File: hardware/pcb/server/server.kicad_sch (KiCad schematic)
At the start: 11 parts

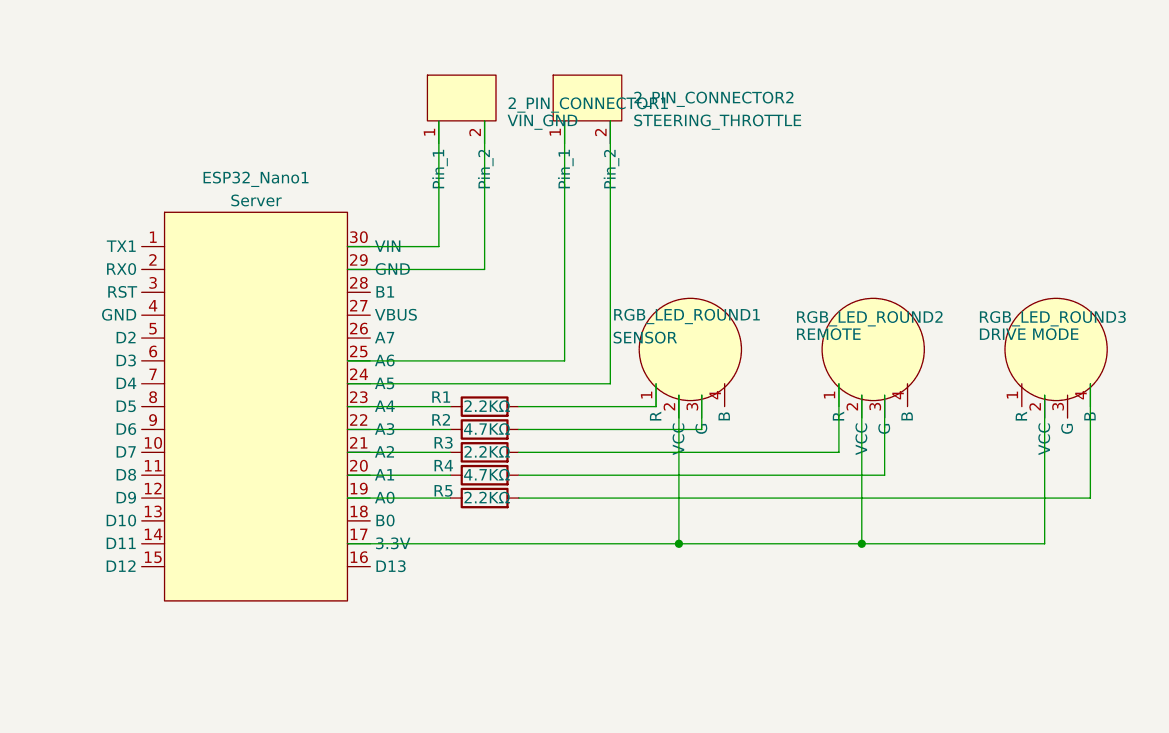
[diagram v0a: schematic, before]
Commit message: hardware/pcb/server: Update pcb pins for the server.
Update the wiring accordingly to use D2-D8 pins.
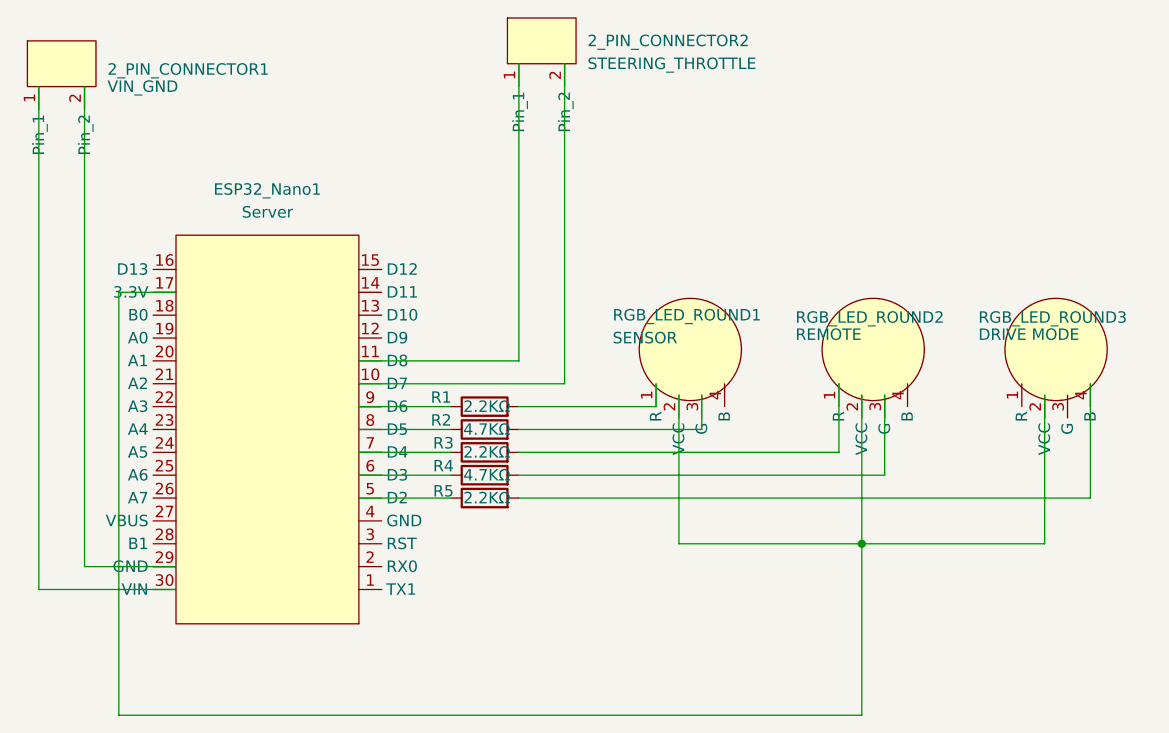
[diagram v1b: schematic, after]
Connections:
- net at ESP32_Nano1.10 (D7): now also 2_PIN_CONNECTOR2.2 (Pin_2)
- net at ESP32_Nano1.11 (D8): now also 2_PIN_CONNECTOR2.1 (Pin_1)
- net at ESP32_Nano1.19 (A0): no longer R5.1
- net at ESP32_Nano1.20 (A1): no longer R4.1
- net at ESP32_Nano1.21 (A2): no longer R3.1
- net at ESP32_Nano1.22 (A3): no longer R2.1
- net at ESP32_Nano1.23 (A4): no longer R1.1
- net at ESP32_Nano1.24 (A5): no longer 2_PIN_CONNECTOR2.2 (Pin_2)
- net at ESP32_Nano1.25 (A6): no longer 2_PIN_CONNECTOR2.1 (Pin_1)
- net at ESP32_Nano1.5 (D2): now also R5.1
- net at ESP32_Nano1.6 (D3): now also R4.1
- net at ESP32_Nano1.7 (D4): now also R3.1
- net at ESP32_Nano1.8 (D5): now also R2.1
- net at ESP32_Nano1.9 (D6): now also R1.1
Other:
- moved on the sheet: 2_PIN_CONNECTOR1, 2_PIN_CONNECTOR2, ESP32_Nano1
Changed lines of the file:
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@@
 	(title_block
 		(title "Autocam Server")
-		(date "2025-03-18")
-		(rev "v0.2")
+		(date "2025-05-21")
+		(rev "v0.3")
 	)
 	(junction
@@
 		(color 0 0 0 0)
 	)
-	(junction
-		(at 165.1 119.38)
-		(diameter 0)
-		(color 0 0 0 0)
-	)
 	(wire
 		(pts
@@
 	(wire
 		(pts
-			(xy 143.51 88.9) (xy 128.27 88.9)
+			(xy 129.54 106.68) (xy 139.7 106.68)
 		)
 		(stroke
@@
 	(wire
 		(pts
-			(xy 128.27 111.76) (xy 139.7 111.76)
-		)
-		(stroke
-			(width 0)
-			(type default)
-		)
-	)
-	(wire
-		(pts
 			(xy 185.42 119.38) (xy 205.74 119.38)
 		)
@@
 	(wire
 		(pts
-			(xy 143.51 72.39) (xy 143.51 88.9)
-		)
-		(stroke
-			(width 0)
-			(type default)
-		)
-	)
-	(wire
-		(pts
-			(xy 157.48 72.39) (xy 157.48 101.6)
-		)
-		(stroke
-			(width 0)
-			(type default)
-		)
-	)
-	(wire
-		(pts
-			(xy 138.43 72.39) (xy 138.43 86.36)
-		)
-		(stroke
-			(width 0)
-			(type default)
-		)
-	)
-	(wire
-		(pts
-			(xy 128.27 114.3) (xy 139.7 114.3)
-		)
-		(stroke
-			(width 0)
-			(type default)
-		)
-	)
-	(wire
-		(pts
-			(xy 128.27 101.6) (xy 157.48 101.6)
-		)
-		(stroke
-			(width 0)
-			(type default)
-		)
-	)
-	(wire
-		(pts
-			(xy 128.27 119.38) (xy 165.1 119.38)
+			(xy 185.42 138.43) (xy 102.87 138.43)
+		)
+		(stroke
+			(width 0)
+			(type default)
+		)
+	)
+	(wire
+		(pts
+			(xy 129.54 109.22) (xy 139.7 109.22)
+		)
+		(stroke
+			(width 0)
+			(type default)
+		)
+	)
+	(wire
+		(pts
+			(xy 102.87 138.43) (xy 102.87 91.44)
+		)
+		(stroke
+			(width 0)
+			(type default)
+		)
+	)
+	(wire
+		(pts
+			(xy 93.98 124.46) (xy 109.22 124.46)
+		)
+		(stroke
+			(width 0)
+			(type default)
+		)
+	)
+	(wire
+		(pts
+			(xy 152.4 101.6) (xy 129.54 101.6)
+		)
+		(stroke
+			(width 0)
+			(type default)
+		)
+	)
+	(wire
+		(pts
+			(xy 129.54 114.3) (xy 139.7 114.3)
+		)
+		(stroke
+			(width 0)
+			(type default)
+		)
+	)
+	(wire
+		(pts
+			(xy 152.4 66.04) (xy 152.4 101.6)
+		)
+		(stroke
+			(width 0)
+			(type default)
+		)
+	)
+	(wire
+		(pts
+			(xy 185.42 119.38) (xy 185.42 138.43)
 		)
 		(stroke
@@
 	(wire
 		(pts
+			(xy 102.87 91.44) (xy 109.22 91.44)
+		)
+		(stroke
+			(width 0)
+			(type default)
+		)
+	)
+	(wire
+		(pts
 			(xy 162.56 101.6) (xy 162.56 104.14)
 		)
@@
 	(wire
 		(pts
-			(xy 138.43 86.36) (xy 128.27 86.36)
-		)
-		(stroke
-			(width 0)
-			(type default)
-		)
-	)
-	(wire
-		(pts
 			(xy 182.88 101.6) (xy 182.88 109.22)
 		)
@@
 	(wire
 		(pts
+			(xy 93.98 68.58) (xy 93.98 124.46)
+		)
+		(stroke
+			(width 0)
+			(type default)
+		)
+	)
+	(wire
+		(pts
 			(xy 147.32 111.76) (xy 187.96 111.76)
 		)
@@
 	(wire
 		(pts
-			(xy 139.7 104.14) (xy 128.27 104.14)
-		)
-		(stroke
-			(width 0)
-			(type default)
-		)
-	)
-	(wire
-		(pts
-			(xy 139.7 109.22) (xy 128.27 109.22)
+			(xy 147.32 66.04) (xy 147.32 99.06)
+		)
+		(stroke
+			(width 0)
+			(type default)
+		)
+	)
+	(wire
+		(pts
+			(xy 99.06 68.58) (xy 99.06 121.92)
 		)
 		(stroke
@@
 	(wire
 		(pts
-			(xy 152.4 72.39) (xy 152.4 99.06)
-		)
-		(stroke
-			(width 0)
-			(type default)
-		)
-	)
-	(wire
-		(pts
-			(xy 128.27 106.68) (xy 139.7 106.68)
+			(xy 129.54 111.76) (xy 139.7 111.76)
 		)
 		(stroke
@@
 	(wire
 		(pts
+			(xy 147.32 99.06) (xy 129.54 99.06)
+		)
+		(stroke
+			(width 0)
+			(type default)
+		)
+	)
+	(wire
+		(pts
 			(xy 187.96 102.87) (xy 187.96 111.76)
 		)
@@
 	(wire
 		(pts
-			(xy 152.4 99.06) (xy 128.27 99.06)
+			(xy 129.54 104.14) (xy 139.7 104.14)
 		)
 		(stroke
@@
 		(pts
 			(xy 147.32 114.3) (xy 210.82 114.3)
+		)
+		(stroke
+			(width 0)
+			(type default)
+		)
+	)
+	(wire
+		(pts
+			(xy 99.06 121.92) (xy 109.22 121.92)
 		)
 		(stroke
@@
 	(symbol
 		(lib_id "Autocam:2_PIN_Connector")
-		(at 140.97 69.85 0)
+		(at 96.52 66.04 0)
 		(unit 1)
 		(exclude_from_sim no)
@@
 		(on_board yes)
 		(dnp no)
-		(fields_autoplaced yes)
 		(property "Reference" "2_PIN_CONNECTOR1"
-			(at 146.05 70.4849 0)
+			(at 101.6 66.6749 0)
 			(effects
 				(font
@@
 		)
 		(property "Value" "VIN_GND"
-			(at 146.05 72.39 0)
+			(at 101.6 68.58 0)
 			(effects
 				(font
@@
 		)
 		(property "Footprint" "Autocam:2-PIN Connector"
-			(at 140.97 69.85 0)
+			(at 96.52 66.04 0)
 			(effects
 				(font
@@
 		)
 		(property "Datasheet" ""
-			(at 140.97 69.85 0)
+			(at 96.52 66.04 0)
 			(effects
 				(font
@@
 		)
 		(property "Description" ""
-			(at 140.97 69.85 0)
+			(at 96.52 66.04 0)
 			(effects
 				(font
@@
 	(symbol
 		(lib_id "Autocam:Arduino_ESP32_Nano")
-		(at 118.11 102.87 0)
+		(at 119.38 107.95 180)
 		(unit 1)
 		(exclude_from_sim no)
@@
 		(fields_autoplaced yes)
 		(property "Reference" "ESP32_Nano1"
-			(at 118.11 78.74 0)
+			(at 119.38 80.01 0)
 			(effects
 				(font
@@
 		)
 		(property "Value" "Server"
-			(at 118.11 81.28 0)
+			(at 119.38 82.55 0)
 			(effects
 				(font
@@
 		)
 		(property "Footprint" "Autocam:Arduino ESP32 Nano"
-			(at 118.11 92.71 0)
+			(at 119.38 118.11 0)
 			(effects
 				(font
@@
 		)
 		(property "Datasheet" ""
-			(at 118.11 92.71 0)
+			(at 119.38 118.11 0)
 			(effects
 				(font
@@
 		)
 		(property "Description" ""
-			(at 118.11 92.71 0)
+			(at 119.38 118.11 0)
 			(effects
 				(font
@@
 	(symbol
 		(lib_id "Autocam:2_PIN_Connector")
-		(at 154.94 69.85 0)
+		(at 149.86 63.5 0)
 		(unit 1)
 		(exclude_from_sim no)
@@
 		(fields_autoplaced yes)
 		(property "Reference" "2_PIN_CONNECTOR2"
-			(at 160.02 69.8499 0)
+			(at 154.94 63.4999 0)
 			(effects
 				(font
@@
 		)
 		(property "Value" "STEERING_THROTTLE"
-			(at 160.02 72.3899 0)
+			(at 154.94 66.0399 0)
 			(effects
 				(font
@@
 		)
 		(property "Footprint" "Autocam:2-PIN Connector"
-			(at 154.94 69.85 0)
+			(at 149.86 63.5 0)
 			(effects
 				(font
@@
 		)
 		(property "Datasheet" ""
-			(at 154.94 69.85 0)
+			(at 149.86 63.5 0)
 			(effects
 				(font
@@
 		)
 		(property "Description" ""
-			(at 154.94 69.85 0)
-			(effects
-				(font
+			(at 149.86 63.5 0)
+			(effects
+				(font
